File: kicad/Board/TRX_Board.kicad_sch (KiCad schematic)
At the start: 61 parts, among them J1 Conn_02x08_Odd_Even, J2 SMA, J3 Conn_01x03, J4 Conn_01x03, Q1 BSN20, Q2 BSN20, Q3 BSN20, U1 AP1117-33, U2 LM386, U3 DRA818U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

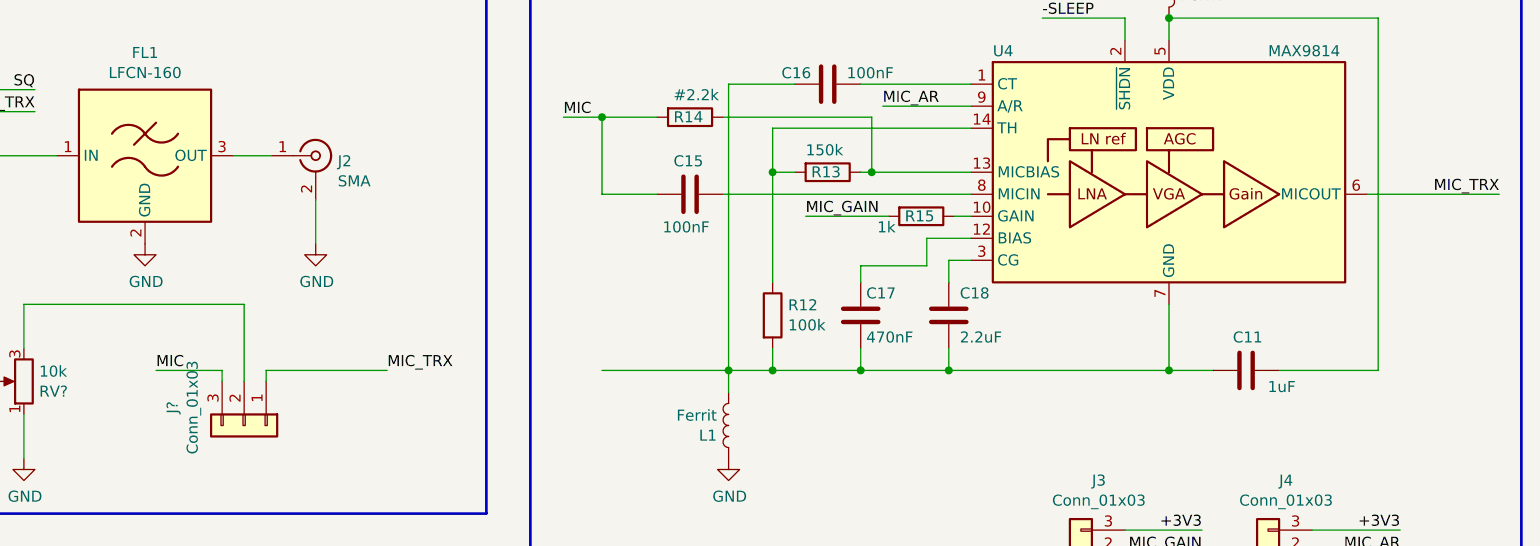
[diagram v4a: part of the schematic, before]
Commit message: MIC input jumper labels changed
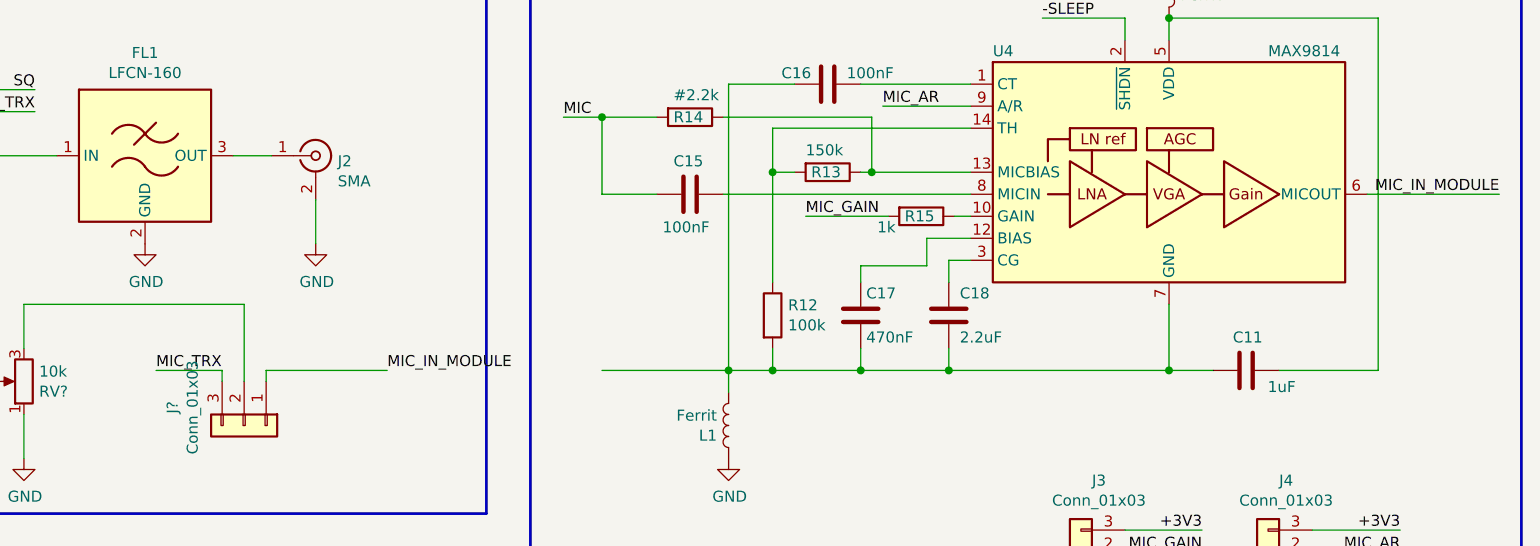
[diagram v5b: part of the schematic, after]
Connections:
- net MIC: no longer J?.3 (Pin_3)
- net MIC_TRX: now also J?.3 (Pin_3); no longer J?.1 (Pin_1), U4.6 (MICOUT)
- new net MIC_IN_MODULE: J?.1 (Pin_1), U4.6 (MICOUT)
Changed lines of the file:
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@@
     (effects (font (size 1.27 1.27)) (justify left bottom))
   )
-  (label "MIC" (at 124.46 72.39 0)
+  (label "MIC_TRX" (at 124.46 72.39 0)
     (effects (font (size 1.27 1.27)) (justify left bottom))
   )
@@
     (effects (font (size 1.27 1.27)) (justify right bottom))
   )
-  (label "MIC_TRX" (at 279.4 52.07 180)
+  (label "MIC_IN_MODULE" (at 279.4 52.07 180)
     (effects (font (size 1.27 1.27)) (justify right bottom))
   )
@@
     (effects (font (size 1.27 1.27)) (justify right bottom))
   )
-  (label "MIC_TRX" (at 151.13 72.39 0)
+  (label "MIC_IN_MODULE" (at 151.13 72.39 0)
     (effects (font (size 1.27 1.27)) (justify left bottom))
   )
